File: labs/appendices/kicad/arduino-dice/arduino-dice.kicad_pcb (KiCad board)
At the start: 2 copper layers, 10 parts, among them IC1 ATMEGA328P-P, P1 CONN_01X02, SW1 SW_PUSH, Y1 16 MHz

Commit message: update pcb
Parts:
- moved R2 30.6 mm to (156.2, 134.6), turned to 270 degrees
- moved SW1 27.1 mm to (149.6, 132.1), turned to 270 degrees
- moved C3 21.5 mm to (154.9, 125.5), turned to 90 degrees
- moved C1 17.7 mm to (164.1, 96.5), turned to 270 degrees
- moved P1 17.7 mm to (161.3, 92.7), turned to 90 degrees
- moved R1 15.1 mm to (161.0, 96.5), turned to 270 degrees
- moved AFF1 14.9 mm to (150.4, 97.3)
- moved Y1 13.1 mm to (154.2, 116.8), turned to 270 degrees
- moved C2 7.19 mm to (154.9, 108.2), turned to 270 degrees
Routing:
- net Net-(C3-Pad2): track 0.00 -> 9.74 mm
- net VCC: track 0.00 -> 6.26 mm
- net Net-(IC1-Pad1): track 0.00 -> 6.18 mm
- net Net-(C2-Pad2): track 0.00 -> 5.80 mm
- net /Button: track 0.00 -> 4.36 mm

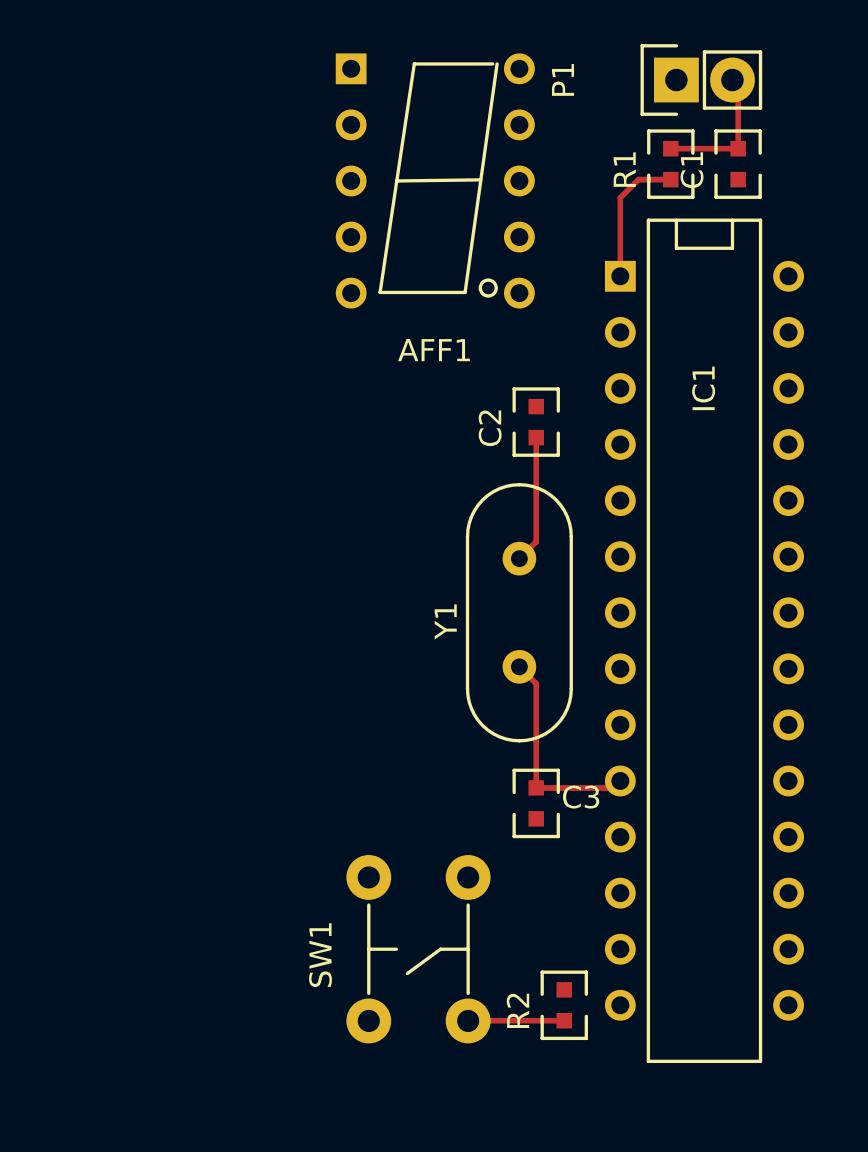
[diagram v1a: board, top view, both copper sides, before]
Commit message: update pcb tutorial
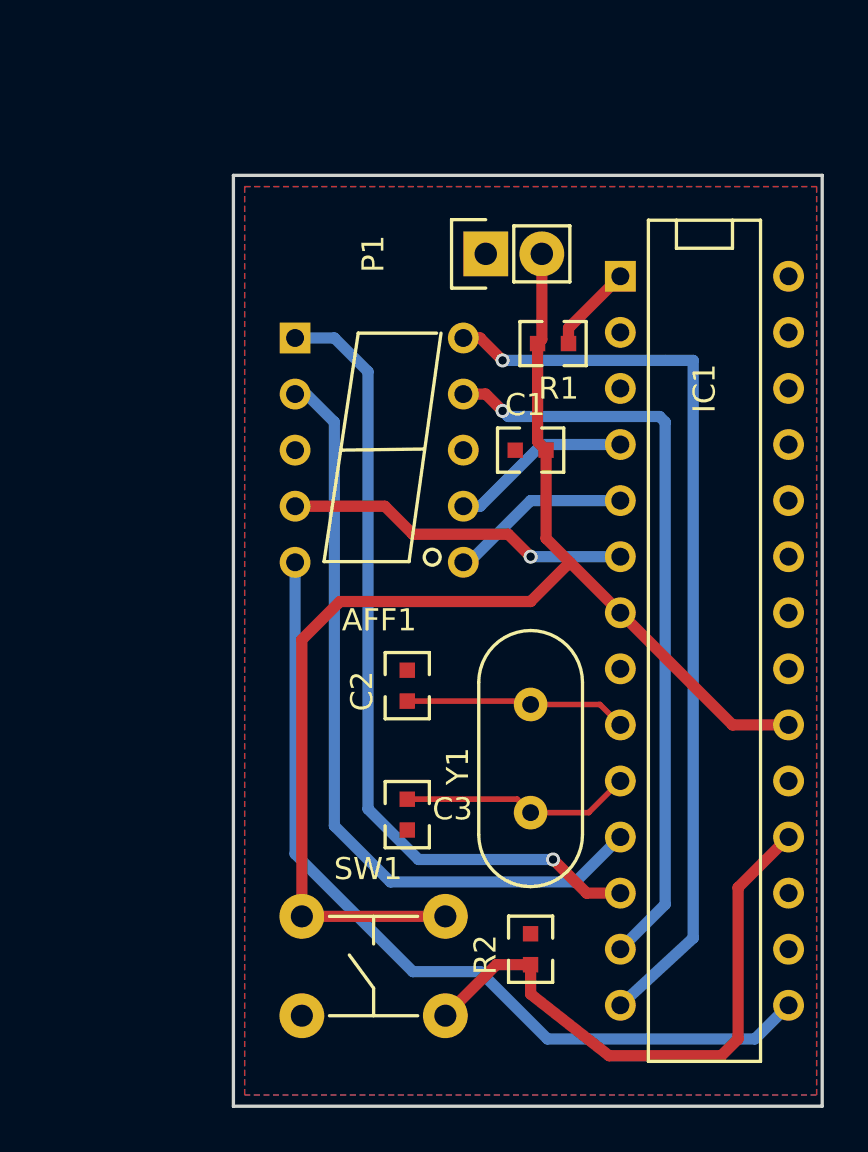
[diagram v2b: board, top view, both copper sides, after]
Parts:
- moved C1 16.0 mm to (154.7, 109.5), turned to 180 degrees
- moved C2 13.3 mm to (149.1, 120.1)
- moved AFF1 12.5 mm to (147.8, 109.5)
- moved P1 11.7 mm to (152.7, 100.6)
- moved R1 9.72 mm to (155.7, 104.6), turned to 0 degrees
- moved Y1 6.62 mm to (154.7, 123.4)
- moved C3 5.86 mm to (149.1, 126.0)
- moved R2 2.96 mm to (154.7, 132.1)
- moved SW1 2.17 mm to (147.6, 132.8), turned to 180 degrees
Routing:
- net VCC: track 6.26 -> 60.5 mm
- net Net-(AFF1-Pad10): track 0.00 -> 41.5 mm, vias 0 -> 1
- net /DP: track 0.00 -> 39.7 mm
- net Net-(AFF1-Pad1): track 0.00 -> 36.8 mm, vias 0 -> 1
- net Net-(AFF1-Pad2): track 0.00 -> 35.4 mm
- net Net-(AFF1-Pad9): track 0.00 -> 34.4 mm, vias 0 -> 1
- net /Button: track 4.36 -> 26.9 mm
- net Net-(AFF1-Pad4): track 0.00 -> 15.7 mm, vias 0 -> 1
- net Net-(AFF1-Pad7): track 0.00 -> 8.27 mm
- net Net-(AFF1-Pad6): track 0.00 -> 8.27 mm
- net Net-(C2-Pad2): track 5.80 -> 10.1 mm
- net Net-(IC1-Pad1): track 6.18 -> 4.02 mm
- net Net-(C3-Pad2): track 9.74 -> 10.9 mm
- added copper zone on B.Cu, net GND
- added copper zone on F.Cu, net GND
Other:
- board outline added: 26.7 x 42.2 mm
